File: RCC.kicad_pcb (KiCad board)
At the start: 2 copper layers, 44.5 x 37 mm, 42 parts, among them J1 Battery, J2 USB_C_Receptacle_USB2.0_16P, J3 Conn_01x07, J4 Conn_01x04_Pin, SW2 SW_Push, U1 BQ24040DGQR, U2 ESD7104MUTAG, U3 TLV75801PDRV, U5 STM32L412KBTx

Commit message: Change PCB stackup to 4 layer
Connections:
- U2 pad 10: unconnected-(U2-NC-Pad10) -> /USB_N
- U2 pad 7: unconnected-(U2-NC-Pad7) -> /VBUS
- U2 pad 9: unconnected-(U2-NC-Pad9) -> /USB_P
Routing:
- added copper zone on In1.Cu, net GND
- added copper zone on In2.Cu, net GND
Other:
- copper layers 2 -> 4

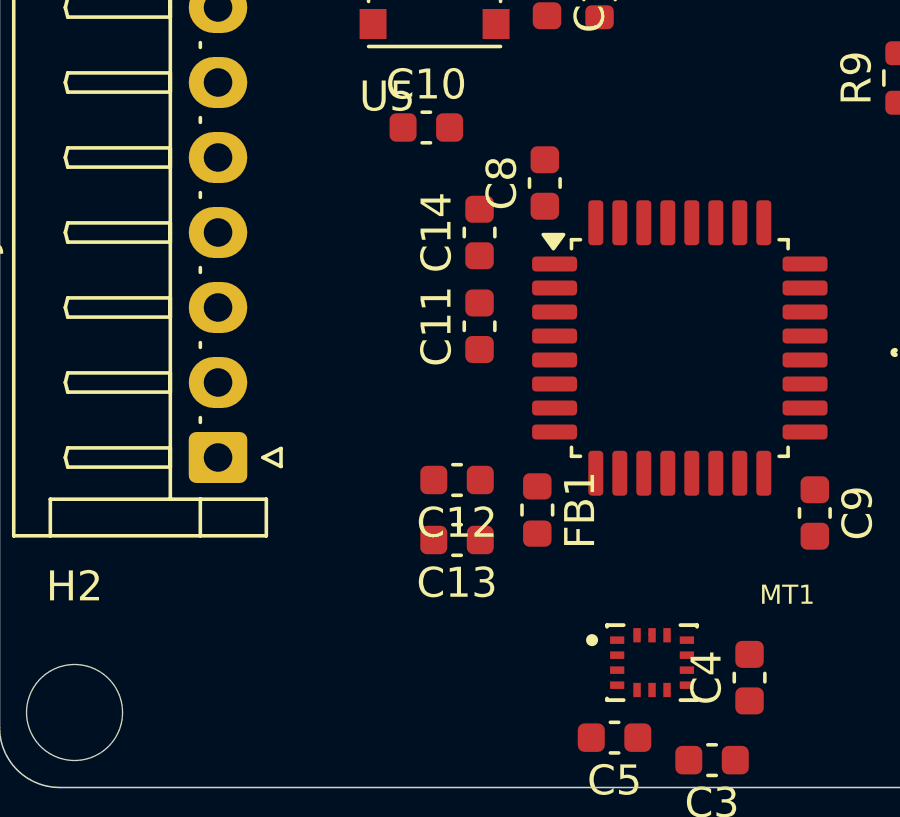
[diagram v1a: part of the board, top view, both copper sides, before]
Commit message: Add crystal in schematic and pcb
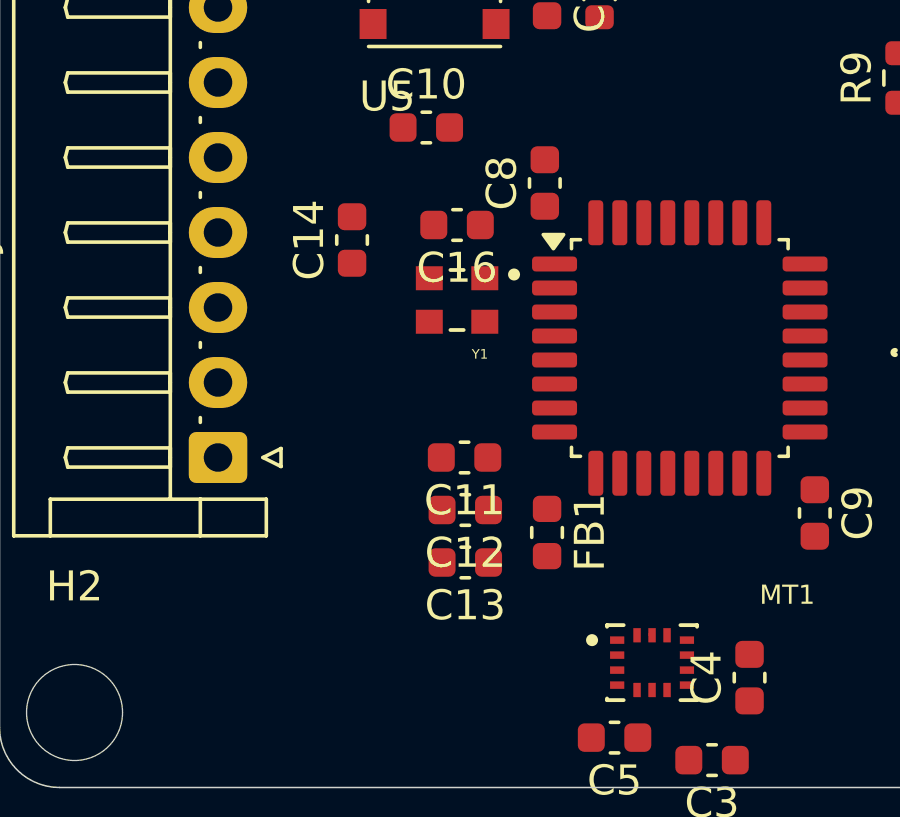
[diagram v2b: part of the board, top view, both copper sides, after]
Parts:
- added C16: 100nF, Capacitor_SMD:C_0603_1608Metric, F.Cu at (115.2, 83.2)
- added Y1: ECS-2520MVQ-480-CN-TR, ECS_2520MVQ_480_CN_TR:OSC_ECS-2520S25-250-FN-TR, F.Cu at (115.2, 85.8)
- moved C11 4.40 mm to (115.5, 91.0), turned to 180 degrees
- moved C14 4.26 mm to (111.8, 83.8)
- moved C12 1.04 mm to (115.5, 92.8)
- moved FB1 0.82 mm to (118.2, 93.5)
- moved C13 0.80 mm to (115.5, 94.5)

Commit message: Finalise PCB and add 3d models
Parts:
- removed R7: 1k5, Resistor_SMD:R_0603_1608Metric
- added D4: LED_Small, LED_SMD:LED_0603_1608Metric, F.Cu at (132.5, 93.2)
- added G***: LOGO, LOGO, F.Cu at (113.0, 69.8)
- C11, C12, C13, C14, C15, FB1, R6, SW2: moved to B.Cu
- J4: footprint Connector_JST:JST_EH_B4B-EH-A_1x04_P2.50mm_Vertical -> Connector_JST:JST_EH_S4B-EH_1x04_P2.50mm_Horizontal
- R11: value 0 -> 1k
- moved C6 18.8 mm to (123.3, 76.6)
- moved D1 18.8 mm to (118.1, 74.1)
- moved R8 18.8 mm to (116.8, 76.6)
- moved U3 18.8 mm to (121.1, 78.2)
- moved C7 18.8 mm to (118.8, 76.6)
- moved R4 18.8 mm to (117.9, 79.0)
- moved R5 18.6 mm to (119.5, 80.6)
- moved J1 14.7 mm to (124.2, 72.2)
- moved C1 9.86 mm to (127.0, 82.3)
- moved J4 8.76 mm to (137.2, 74.2), turned to -90 degrees
- moved R1 8.56 mm to (130.8, 82.8), turned to 0 degrees
- moved C2 6.28 mm to (126.8, 79.1)
- moved SW2 6.27 mm to (112.0, 81.5), turned to 180 degrees
- moved R6 5.94 mm to (117.8, 81.0)
- moved D2 5.82 mm to (133.0, 80.3), turned to 90 degrees
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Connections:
- J2 pad S1: Net-(J2-SHIELD) -> unconnected-(J2-SHIELD-PadS1)_2
- J4 pad 2: /SWDIO -> /SWCLK
- J4 pad 3: /SWCLK -> /SWDIO
- R11 pad 1: Net-(J2-SHIELD) -> Net-(D4-A)
- R11 pad 2: GND -> /TEST_LED
- U2 pad 4: /VBUS -> unconnected-(U2-I/O-Pad4)
- U2 pad 5: unconnected-(U2-I/O-Pad5) -> /VBUS
- U2 pad 6: unconnected-(U2-NC-Pad6) -> /VBUS
- U2 pad 7: /VBUS -> unconnected-(U2-NC-Pad7)
- U5 pad 10: unconnected-(U5-PA4-Pad10) -> /GY_INT1
- U5 pad 14: unconnected-(U5-PB0-Pad14) -> /GYRO_CS
- U5 pad 15: unconnected-(U5-PB1-Pad15) -> /GY_INT2
- U5 pad 18: unconnected-(U5-PA8-Pad18) -> /TEST_LED
- U5 pad 27: unconnected-(U5-PB4-Pad27) -> /CHG_STATUS
- U5 pad 28: unconnected-(U5-PB5-Pad28) -> /DIS_RST
- U5 pad 29: unconnected-(U5-PB6-Pad29) -> /DIS_DC
- U5 pad 30: unconnected-(U5-PB7-Pad30) -> /DIS_CS
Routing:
- net +3V3: track 0.00 -> 101.1 mm, vias 0 -> 3
- net GND: track 0.00 -> 53.4 mm, vias 0 -> 22
- net /SCLK: track 0.04 -> 29.4 mm, vias 0 -> 2
- net /MOSI: track 0.00 -> 24.1 mm, vias 0 -> 1
- net /VBAT: track 0.00 -> 21.7 mm
- net /DIS_RST: track 0.00 -> 21.1 mm, vias 0 -> 1
- net /VBUS: track 0.00 -> 20.2 mm
- net /DIS_DC: track 0.00 -> 19.8 mm, vias 0 -> 1
- net /DIS_CS: track 0.00 -> 19.3 mm, vias 0 -> 1
- net /CHG_STATUS: track 0.00 -> 16.0 mm, vias 0 -> 2
- net /SWCLK: track 0.00 -> 14.1 mm, vias 0 -> 1
- net /SWDIO: track 0.00 -> 13.1 mm, vias 0 -> 1
- net /USB_N: track 0.00 -> 13.0 mm
- net /USB_P: track 0.00 -> 13.0 mm
- net /SW_BOOT0: track 0.00 -> 8.60 mm
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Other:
- board text added: "3V3"
- board text added: "BATTERY"
- board text added: "BOOT"
- board text added: "BoJoe"
- board text added: "CHG"
- board text added: "DEBUG"
- board text added: "DISPLAY"
- board text added: "Dashidaa"
- board text added: "GYRO"
- board text added: "POW"
- board text added: "blinky"

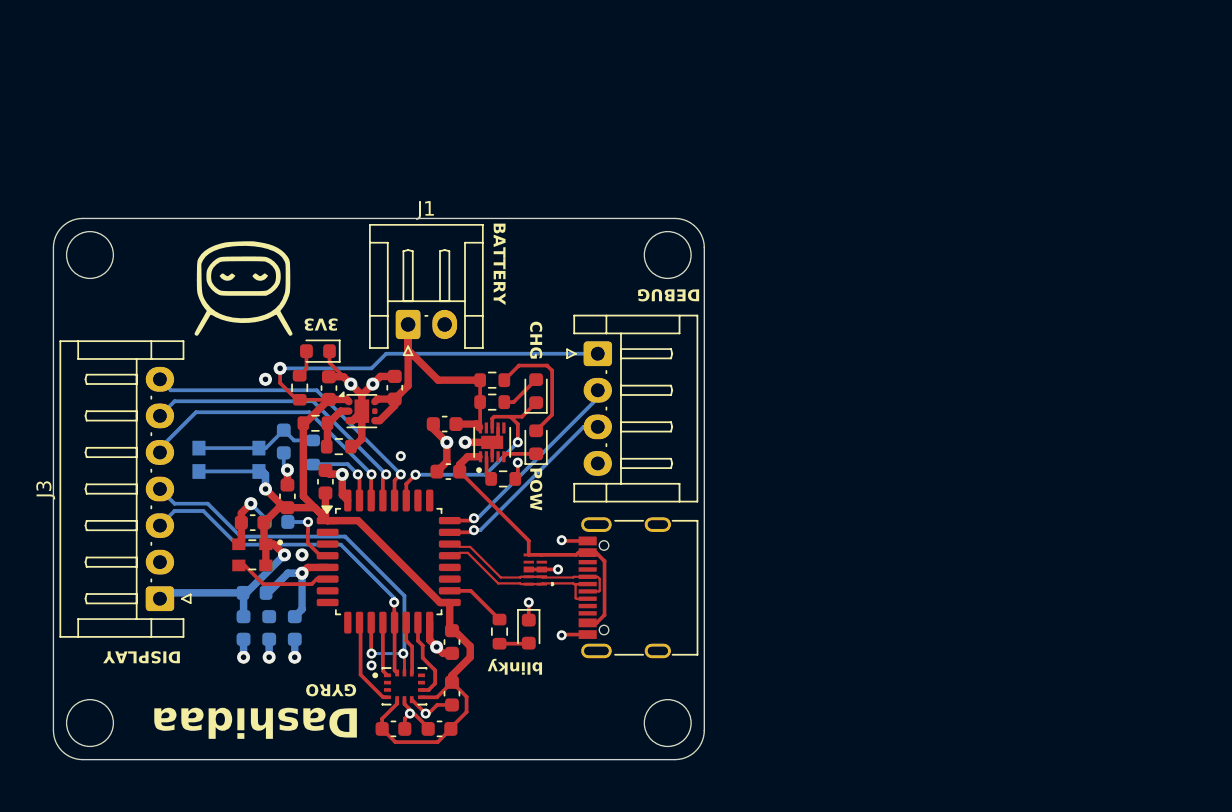
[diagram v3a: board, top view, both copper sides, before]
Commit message: Change connectors to jst-ph
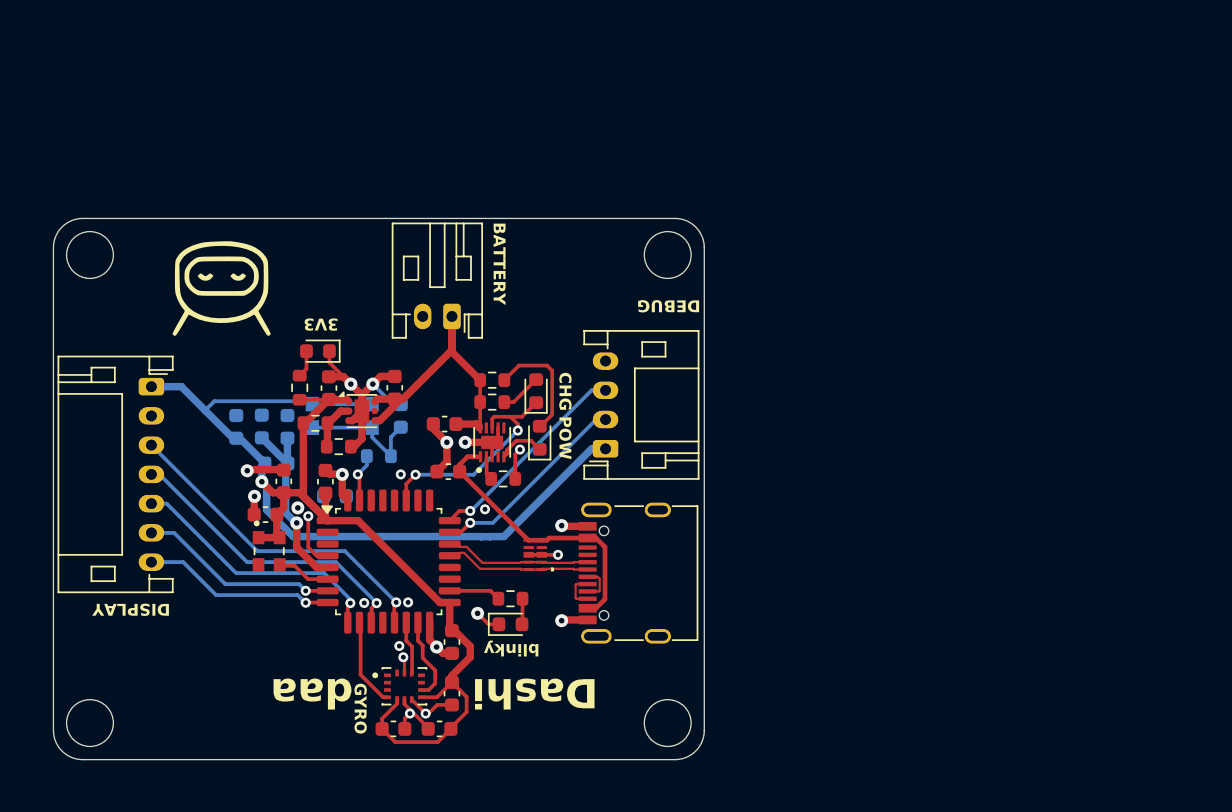
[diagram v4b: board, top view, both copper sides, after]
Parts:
- C14, C15, C16, C8, C9: value 100nF -> 0.1uF
- J1: footprint Connector_JST:JST_EH_S2B-EH_1x02_P2.50mm_Horizontal -> Connector_JST:JST_PH_S2B-PH-K_1x02_P2.00mm_Horizontal
- J3: footprint Connector_JST:JST_EH_S7B-EH_1x07_P2.50mm_Horizontal -> Connector_JST:JST_PH_S7B-PH-K_1x07_P2.00mm_Horizontal
- J4: footprint Connector_JST:JST_EH_S4B-EH_1x04_P2.50mm_Horizontal -> Connector_JST:JST_PH_S4B-PH-K_1x04_P2.00mm_Horizontal
- R1: value 540 -> 1k
- moved J3 14.5 mm to (106.7, 76.5), turned to -90 degrees
- moved C12 13.8 mm to (114.2, 79.2), turned to 90 degrees
- moved C11 13.8 mm to (116.0, 79.2), turned to 90 degrees
- moved C13 13.8 mm to (112.5, 79.2), turned to 90 degrees
- moved FB1 8.98 mm to (115.2, 81.8)
- moved SW2 8.31 mm to (119.8, 78.5), turned to 0 degrees
- moved C15 8.19 mm to (123.8, 78.5), turned to 90 degrees
- moved J4 6.52 mm to (137.8, 80.8), turned to 90 degrees
- moved R6 4.51 mm to (122.2, 81.2), turned to 180 degrees
- moved C14 4.37 mm to (119.2, 84.0), turned to 0 degrees
- moved J1 3.05 mm to (127.2, 71.7), turned to 180 degrees
- moved R11 2.37 mm to (131.2, 91.0), turned to 180 degrees
- moved G*** 1.50 mm to (111.5, 69.8)
- moved D4 1.35 mm to (131.2, 92.8), turned to 0 degrees
- moved Y1 1.18 mm to (114.8, 87.8), turned to -90 degrees
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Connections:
- J4 pad 2: /SWCLK -> /SWDIO
- J4 pad 3: /SWDIO -> /SWCLK
- U5 pad 28: /DIS_RST -> unconnected-(U5-PB5-Pad28)
- U5 pad 29: /DIS_DC -> unconnected-(U5-PB6-Pad29)
- U5 pad 30: /DIS_CS -> unconnected-(U5-PB7-Pad30)
- U5 pad 7: unconnected-(U5-PA1-Pad7) -> /DIS_DC
- U5 pad 8: unconnected-(U5-PA2-Pad8) -> /DIS_RST
- U5 pad 9: unconnected-(U5-PA3-Pad9) -> /DIS_CS
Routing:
- net /DIS_RST: track 21.1 -> 13.2 mm
- net +3V3: track 101.1 -> 108.8 mm, vias 3 -> 1
- net /SCLK: track 29.4 -> 21.7 mm
- net /DIS_DC: track 19.8 -> 13.7 mm
- net +3.3VA: track 8.12 -> 13.1 mm
- net /MISO: track 3.73 -> 0.00 mm
- net /HSE_IN: track 6.74 -> 3.68 mm
- net GND: track 53.4 -> 50.5 mm, vias 22 -> 21
- net /BOOT0: track 5.19 -> 3.34 mm
- net /MOSI: track 24.1 -> 22.6 mm
- net /DIS_CS: track 19.3 -> 18.0 mm
- net Net-(D2-K): track 2.28 -> 3.29 mm
- net /VBUS: track 20.2 -> 19.2 mm
- net /NRST: track 4.55 -> 3.69 mm
- net /SWDIO: track 13.1 -> 13.8 mm
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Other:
- board text added: "Dashi"
- board text added: "daa"
- board text removed: "Dashidaa"

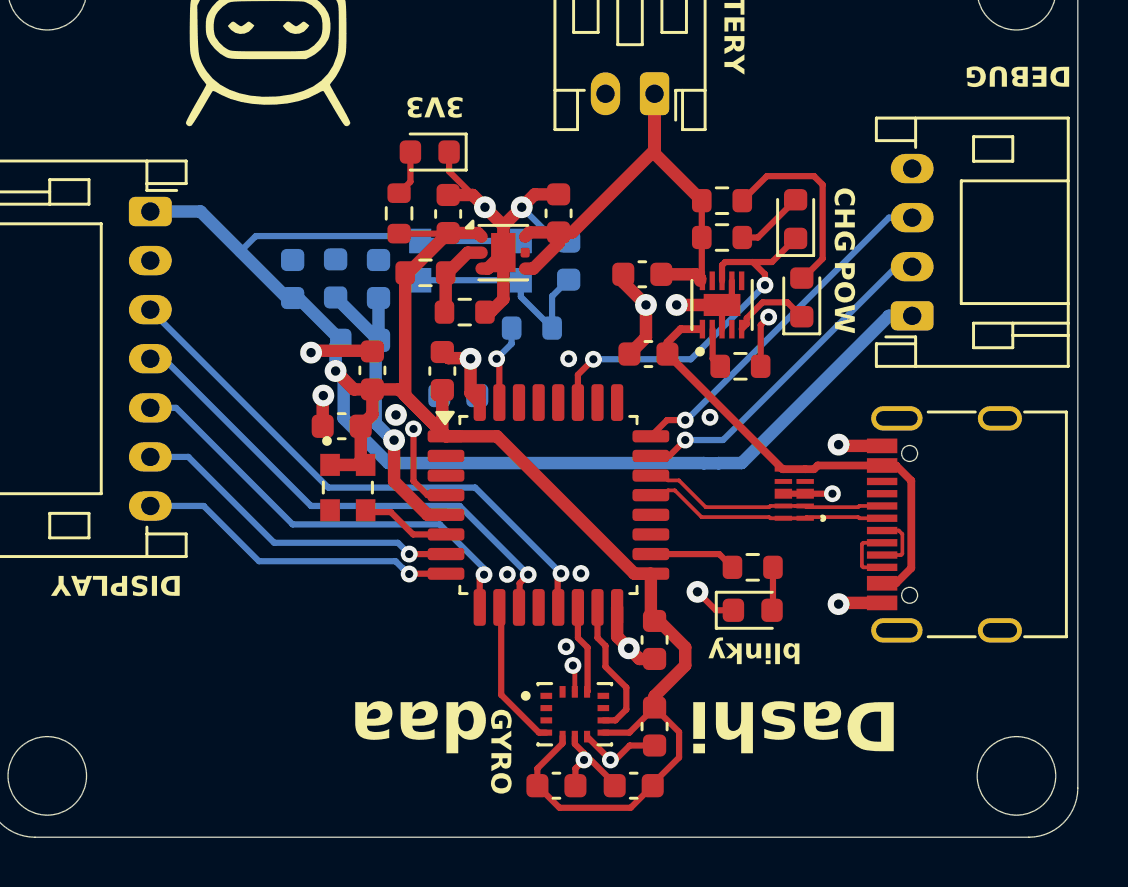
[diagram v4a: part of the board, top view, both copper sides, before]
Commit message: Clean up pcb traces and vias
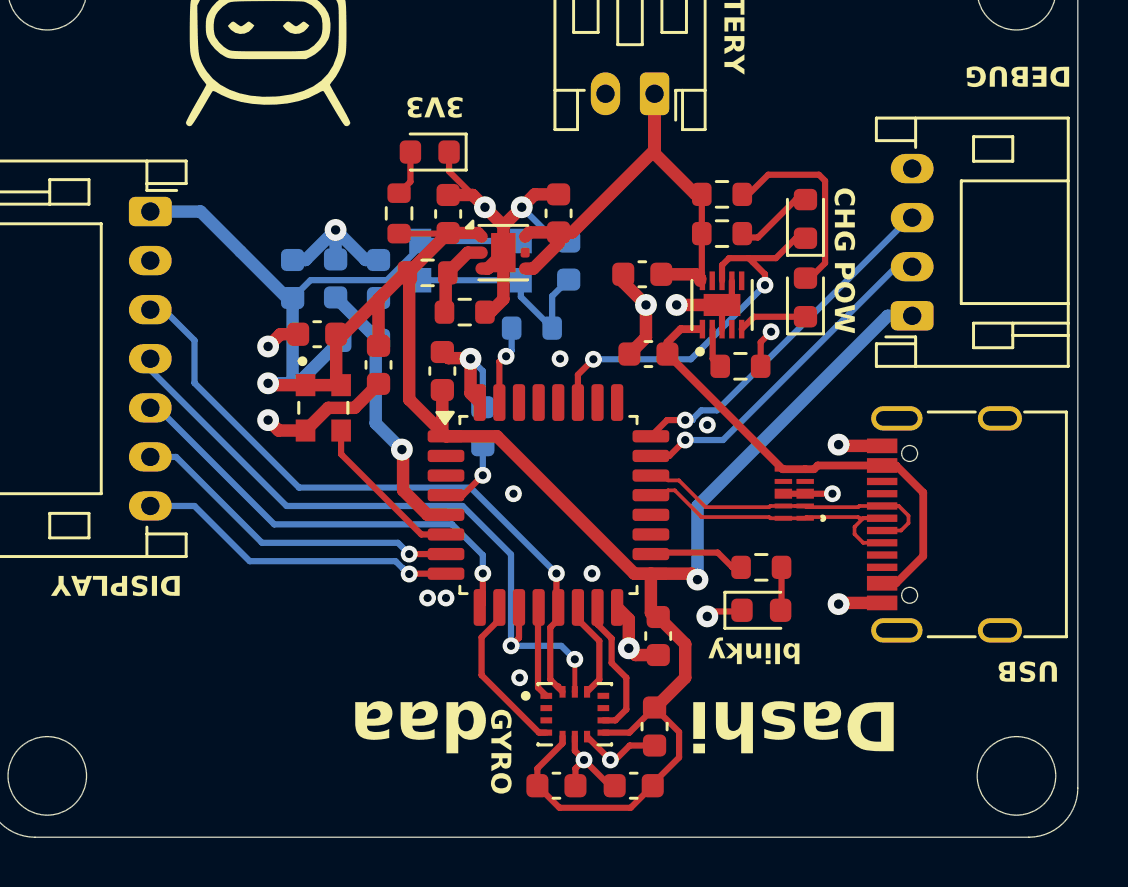
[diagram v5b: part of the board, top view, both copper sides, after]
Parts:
- moved C16 3.88 mm to (113.5, 81.5)
- moved Y1 3.40 mm to (113.8, 84.5)
- moved C14 1.60 mm to (120.2, 85.2), turned to 90 degrees
- moved D3 0.40 mm to (133.4, 76.8)
- moved D4 0.35 mm to (131.6, 92.8)
- moved R11 0.35 mm to (131.6, 91.0)
- moved C10 0.34 mm to (116.0, 82.8), turned to -90 degrees
- moved R9 0.26 mm to (130.0, 75.8)
- moved C9 0.22 mm to (127.4, 93.8)
- moved R10 0.16 mm to (130.0, 77.4)
- moved D2 0.15 mm to (133.4, 80.0)
- moved R4 0.09 mm to (118.0, 79.0)
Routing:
- net GND: track 50.5 -> 61.0 mm, vias 21 -> 23
- net +3V3: track 108.8 -> 99.9 mm, vias 1 -> 2
- net /SCLK: track 21.7 -> 27.9 mm
- net /MOSI: track 22.6 -> 27.2 mm
- net /MISO: track 0.00 -> 3.75 mm
- net /HSE_IN: track 3.68 -> 6.59 mm
- net /NRST: track 3.69 -> 3.06 mm
- net /CHG_STATUS: track 15.5 -> 16.1 mm
- net /GY_INT1: track 6.07 -> 6.67 mm
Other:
- board text added: "USB"
